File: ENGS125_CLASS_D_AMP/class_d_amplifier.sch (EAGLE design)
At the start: 21 parts, among them J1 BANANA_JACK_CT3151, J2 BANANA_JACK_CT3151, J3 BANANA_JACK_CT3151, J4 BANANA_JACK_CT3151, J5 BANANA_JACK_CT3151, J6 BANANA_JACK_CT3151, M1 AUIRLR024ZTRL, M2 AUIRLR024ZTRL, U1 LTC6992TSOT-23, U2 LTC4449

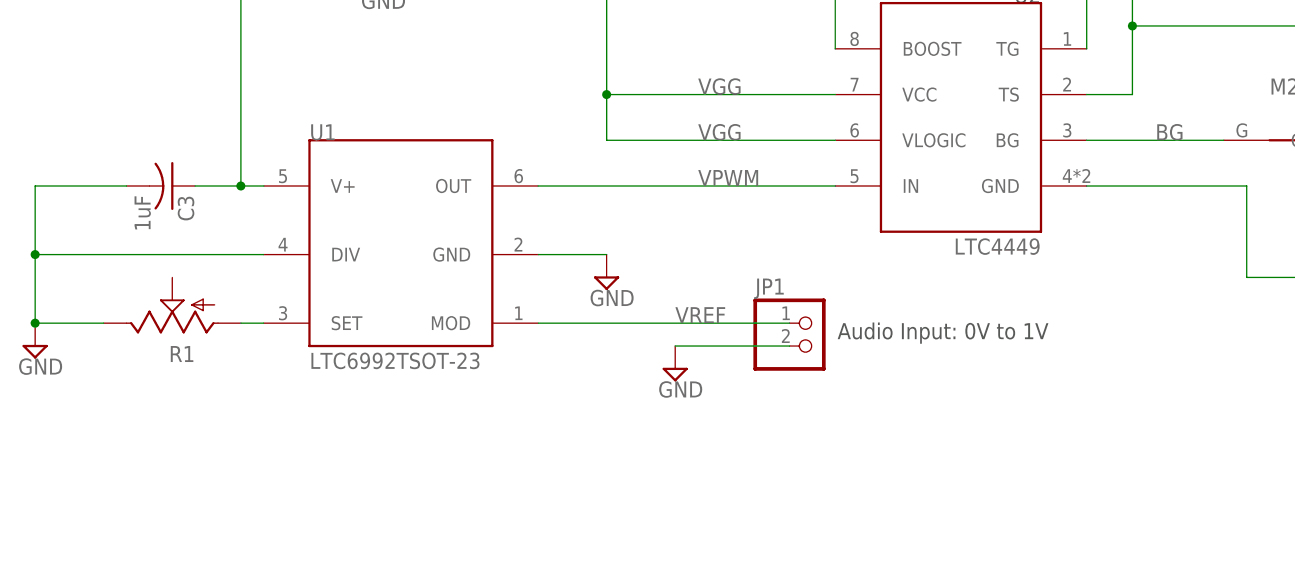
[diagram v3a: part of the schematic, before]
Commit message: Added pin header for PWM output probe
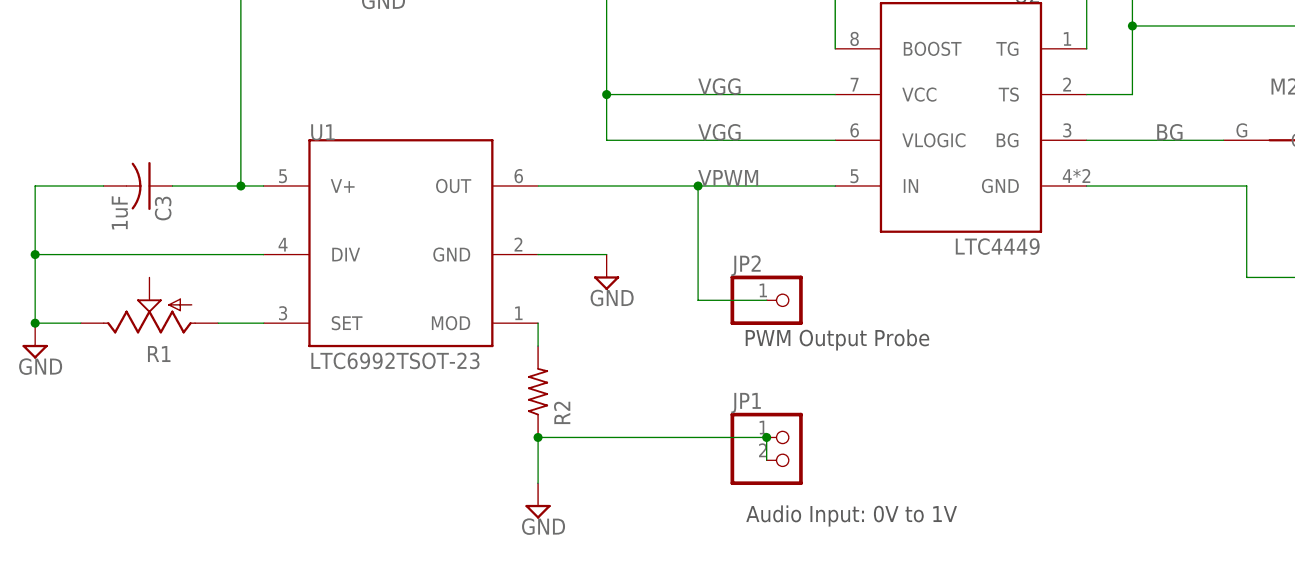
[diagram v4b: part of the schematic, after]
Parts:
- added JP2: (no value), Engs125_lib_UPDATEFeb22:PINHD-1X1
- added R2: R-US, Engs125_lib_UPDATEFeb22:R-US
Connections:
- removed net VREF: JP1.1, U1.MOD
- new net N$4: R2.2, U1.MOD
- net GND: now also JP1.1, R2.1
- net VPWM: now also JP2.1
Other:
- note added: "PWM Output Probe"
- moved on the sheet: C3, JP1, R1
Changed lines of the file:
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@@
 <part name="U1" library="Engs125_lib_UPDATEFeb22" deviceset="LTC6992" device="TSOT-23"/>
 <part name="R1" library="Engs125_lib_UPDATEFeb22" deviceset="TRIM_US-" device="CT6"/>
+<part name="R2" library="Engs125_lib_UPDATEFeb22" deviceset="R-US" device="" value=""/>
+<part name="JP2" library="Engs125_lib_UPDATEFeb22" deviceset="PINHD-1X1" device=""/>
 </parts>
 <sheets>
@@
 @1.5A DC load current (4Ω load)</text>
 <text x="15.24" y="132.08" size="1.778" layer="97">Gate Supply: 5V</text>
-<text x="68.834" y="43.942" size="1.778" layer="97">Audio Input: 0V to 1V</text>
+<text x="58.674" y="23.622" size="1.778" layer="97">Audio Input: 0V to 1V</text>
+<text x="58.42" y="43.18" size="1.778" layer="97">PWM Output Probe</text>
 </plain>
 <instances>
@@
 <attribute name="VALUE" x="-22.225" y="40.005" size="1.778" layer="96"/>
 </instance>
-<instance part="C3" gate="G$1" x="-5.08" y="60.96" smashed="yes" rot="R270">
-<attribute name="NAME" x="-4.445" y="59.944" size="1.778" layer="95" rot="R270"/>
-<attribute name="VALUE" x="-9.271" y="59.944" size="1.778" layer="96" rot="R270"/>
+<instance part="C3" gate="G$1" x="-7.62" y="60.96" smashed="yes" rot="R270">
+<attribute name="NAME" x="-6.985" y="59.944" size="1.778" layer="95" rot="R270"/>
+<attribute name="VALUE" x="-11.811" y="59.944" size="1.778" layer="96" rot="R270"/>
 </instance>
 <instance part="C4" gate="G$1" x="17.78" y="93.98" smashed="yes">
@@
 <attribute name="VALUE" x="41.275" y="47.625" size="1.778" layer="96"/>
 </instance>
-<instance part="SUPPLY3" gate="GND" x="50.8" y="40.64" smashed="yes">
-<attribute name="VALUE" x="48.895" y="37.465" size="1.778" layer="96"/>
+<instance part="SUPPLY3" gate="GND" x="35.56" y="25.4" smashed="yes">
+<attribute name="VALUE" x="33.655" y="22.225" size="1.778" layer="96"/>
 </instance>
 <instance part="SUPPLY4" gate="GND" x="25.4" y="106.68" smashed="yes">
@@
 <attribute name="VALUE" x="168.656" y="66.929" size="1.778" layer="96"/>
 </instance>
-<instance part="JP1" gate="G$1" x="66.04" y="43.18" smashed="yes">
-<attribute name="NAME" x="59.69" y="48.895" size="1.778" layer="95"/>
-<attribute name="VALUE" x="59.69" y="38.1" size="1.778" layer="96"/>
+<instance part="JP1" gate="G$1" x="63.5" y="30.48" smashed="yes">
+<attribute name="NAME" x="57.15" y="36.195" size="1.778" layer="95"/>
+<attribute name="VALUE" x="57.15" y="25.4" size="1.778" layer="96"/>
 </instance>
 <instance part="J1" gate="G$1" x="17.78" y="119.38" smashed="yes" rot="R270">
@@
 <attribute name="VALUE" x="10.16" y="40.64" size="1.778" layer="96"/>
 </instance>
-<instance part="R1" gate="G$1" x="-5.08" y="45.72" smashed="yes" rot="R90">
-<attribute name="NAME" x="-2.54" y="43.18" size="1.778" layer="95" rot="R180"/>
-<attribute name="VALUE" x="-2.54" y="43.18" size="1.778" layer="96" rot="R180"/>
+<instance part="R1" gate="G$1" x="-7.62" y="45.72" smashed="yes" rot="R90">
+<attribute name="NAME" x="-5.08" y="43.18" size="1.778" layer="95" rot="R180"/>
+<attribute name="VALUE" x="-5.08" y="43.18" size="1.778" layer="96" rot="R180"/>
+</instance>
+<instance part="R2" gate="G$1" x="35.56" y="38.1" smashed="yes" rot="R90">
+<attribute name="NAME" x="39.1414" y="34.29" size="1.778" layer="95" rot="R90"/>
+<attribute name="VALUE" x="38.862" y="34.29" size="1.778" layer="96" rot="R90"/>
+</instance>
+<instance part="JP2" gate="G$1" x="63.5" y="48.26" smashed="yes">
+<attribute name="NAME" x="57.15" y="51.435" size="1.778" layer="95"/>
+<attribute name="VALUE" x="57.15" y="43.18" size="1.778" layer="96"/>
 </instance>
 </instances>
@@
 <net name="N$1" class="0">
 <segment>
-<wire x1="5.08" y1="45.72" x2="2.54" y2="45.72" width="0.1524" layer="91"/>
+<wire x1="5.08" y1="45.72" x2="0" y2="45.72" width="0.1524" layer="91"/>
 <pinref part="U1" gate="G$1" pin="SET"/>
 <pinref part="R1" gate="G$1" pin="A"/>
@@
 <segment>
 <pinref part="SUPPLY1" gate="GND" pin="GND"/>
-<wire x1="-12.7" y1="45.72" x2="-20.32" y2="45.72" width="0.1524" layer="91"/>
+<wire x1="-15.24" y1="45.72" x2="-20.32" y2="45.72" width="0.1524" layer="91"/>
 <wire x1="5.08" y1="53.34" x2="-20.32" y2="53.34" width="0.1524" layer="91"/>
 <wire x1="-20.32" y1="53.34" x2="-20.32" y2="45.72" width="0.1524" layer="91"/>
 <junction x="-20.32" y="45.72"/>
 <pinref part="C3" gate="G$1" pin="2"/>
-<wire x1="-10.16" y1="60.96" x2="-20.32" y2="60.96" width="0.1524" layer="91"/>
+<wire x1="-12.7" y1="60.96" x2="-20.32" y2="60.96" width="0.1524" layer="91"/>
 <wire x1="-20.32" y1="60.96" x2="-20.32" y2="53.34" width="0.1524" layer="91"/>
 <junction x="-20.32" y="53.34"/>
@@
 </segment>
 <segment>
-<pinref part="SUPPLY3" gate="GND" pin="GND"/>
-<wire x1="50.8" y1="43.18" x2="63.5" y2="43.18" width="0.1524" layer="91"/>
-<pinref part="JP1" gate="G$1" pin="2"/>
-</segment>
-<segment>
 <pinref part="J2" gate="G$1" pin="IN"/>
 <pinref part="SUPPLY4" gate="GND" pin="GND"/>
@@
 <wire x1="137.16" y1="137.16" x2="137.16" y2="134.62" width="0.1524" layer="91"/>
 </segment>
+<segment>
+<pinref part="JP1" gate="G$1" pin="2"/>
+<pinref part="JP1" gate="G$1" pin="1"/>
+<wire x1="60.96" y1="33.02" x2="60.96" y2="30.48" width="0.1524" layer="91"/>
+<pinref part="R2" gate="G$1" pin="1"/>
+<wire x1="35.56" y1="33.02" x2="60.96" y2="33.02" width="0.1524" layer="91"/>
+<junction x="60.96" y="33.02"/>
+<pinref part="SUPPLY3" gate="GND" pin="GND"/>
+<wire x1="35.56" y1="33.02" x2="35.56" y2="27.94" width="0.1524" layer="91"/>
+<junction x="35.56" y="33.02"/>
+</segment>
 </net>
 <net name="VGG" class="0">
@@
 <pinref part="C3" gate="G$1" pin="1"/>
 <wire x1="5.08" y1="60.96" x2="2.54" y2="60.96" width="0.1524" layer="91"/>
-<wire x1="2.54" y1="60.96" x2="-2.54" y2="60.96" width="0.1524" layer="91"/>
+<wire x1="2.54" y1="60.96" x2="-5.08" y2="60.96" width="0.1524" layer="91"/>
 <wire x1="2.54" y1="60.96" x2="2.54" y2="99.06" width="0.1524" layer="91"/>
 <wire x1="2.54" y1="99.06" x2="17.78" y2="99.06" width="0.1524" layer="91"/>
@@
 <segment>
 <pinref part="U2" gate="G$1" pin="IN"/>
-<wire x1="35.56" y1="60.96" x2="68.58" y2="60.96" width="0.1524" layer="91"/>
+<wire x1="35.56" y1="60.96" x2="53.34" y2="60.96" width="0.1524" layer="91"/>
 <label x="53.34" y="60.96" size="1.778" layer="95"/>
 <pinref part="U1" gate="G$1" pin="OUT"/>
+<pinref part="JP2" gate="G$1" pin="1"/>
+<wire x1="53.34" y1="60.96" x2="68.58" y2="60.96" width="0.1524" layer="91"/>
+<wire x1="53.34" y1="60.96" x2="53.34" y2="48.26" width="0.1524" layer="91"/>
+<wire x1="53.34" y1="48.26" x2="60.96" y2="48.26" width="0.1524" layer="91"/>
+<junction x="53.34" y="60.96"/>
 </segment>
 </net>
@@
 </segment>
 </net>
-<net name="VREF" class="0">
-<segment>
-<wire x1="35.56" y1="45.72" x2="63.5" y2="45.72" width="0.1524" layer="91"/>
-<label x="50.8" y="45.72" size="1.778" layer="95"/>
-<pinref part="JP1" gate="G$1" pin="1"/>
-<pinref part="U1" gate="G$1" pin="MOD"/>
-</segment>
-</net>
 <net name="N$3" class="0">
 <segment>
@@
 </segment>
 </net>
+<net name="N$4" class="0">
+<segment>
+<pinref part="U1" gate="G$1" pin="MOD"/>
+<pinref part="R2" gate="G$1" pin="2"/>
+<wire x1="35.56" y1="45.72" x2="35.56" y2="43.18" width="0.1524" layer="91"/>
+</segment>
+</net>

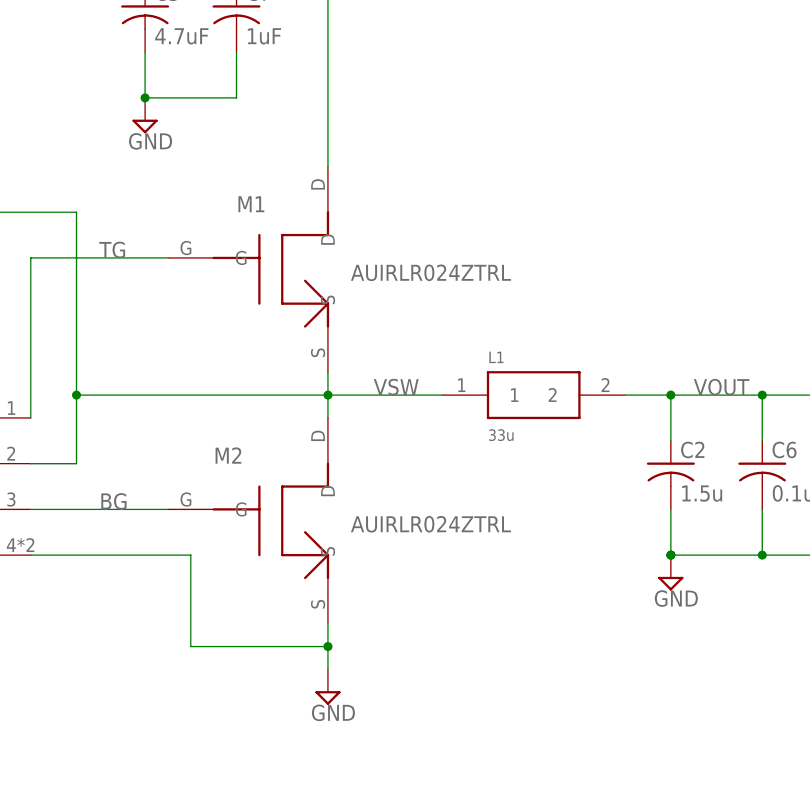
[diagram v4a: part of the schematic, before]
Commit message: Added footprint for switch. Added switch to schematic.
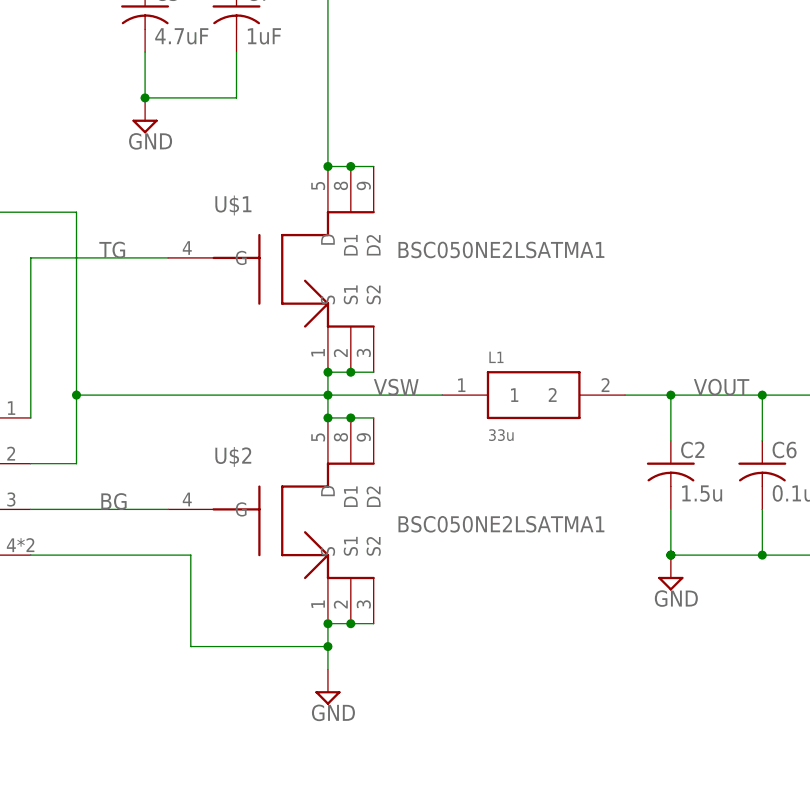
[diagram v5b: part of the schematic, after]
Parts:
- removed M1, M2: AUIRLR024ZTRL, Engs125_library:MOSFET_DPAK
- added U$1, U$2: BSC050NE2LSATMA1, Engs125_lib_UPDATEFeb22:BSC050NE2LSATMA1
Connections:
- net BG: now also U$2.G; no longer M2.G
- net GND: now also U$2.S, U$2.S1, U$2.S2; no longer M2.S
- net TG: now also U$1.G; no longer M1.G
- net VIN: now also U$1.D, U$1.D1, U$1.D2; no longer M1.D
- net VSW: now also U$1.S, U$1.S1, U$1.S2, U$2.D, U$2.D1, U$2.D2; no longer M1.S, M2.D
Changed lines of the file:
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@@
 <part name="C6" library="Engs125_library" deviceset="C-US" device="" value="0.1u"/>
 <part name="D1" library="Engs125_library" deviceset="DIODE" device="" value="1N5819"/>
-<part name="M1" library="Engs125_library" deviceset="MOSFET_DPAK" device="" value="AUIRLR024ZTRL"/>
-<part name="M2" library="Engs125_library" deviceset="MOSFET_DPAK" device="" value="AUIRLR024ZTRL"/>
 <part name="L1" library="Engs125_library" deviceset="SER2900" device="SER" value="33u"/>
 <part name="SUPPLY2" library="Engs125_library" deviceset="GND" device=""/>
@@
 <part name="R2" library="Engs125_lib_UPDATEFeb22" deviceset="R-US" device="" value=""/>
 <part name="JP2" library="Engs125_lib_UPDATEFeb22" deviceset="PINHD-1X1" device=""/>
+<part name="U$1" library="Engs125_lib_UPDATEFeb22" deviceset="BSC050NE2LSATMA1" device=""/>
+<part name="U$2" library="Engs125_lib_UPDATEFeb22" deviceset="BSC050NE2LSATMA1" device=""/>
 </parts>
 <sheets>
@@
 <attribute name="NAME" x="55.88" y="88.9" size="1.778" layer="95"/>
 </instance>
-<instance part="M1" gate="G$1" x="124.46" y="93.98" smashed="yes">
-<attribute name="NAME" x="119.38" y="99.06" size="1.778" layer="95"/>
-<attribute name="VALUE" x="132.08" y="91.44" size="1.778" layer="96"/>
-</instance>
-<instance part="M2" gate="G$1" x="124.46" y="66.04" smashed="yes">
-<attribute name="NAME" x="116.84" y="71.12" size="1.778" layer="95"/>
-<attribute name="VALUE" x="132.08" y="63.5" size="1.778" layer="96"/>
-</instance>
 <instance part="L1" gate="G$1" x="152.4" y="78.74" smashed="yes">
 <attribute name="VALUE" x="147.32" y="73.66" size="1.27" layer="96"/>
@@
 <attribute name="NAME" x="57.15" y="51.435" size="1.778" layer="95"/>
 <attribute name="VALUE" x="57.15" y="43.18" size="1.778" layer="96"/>
+</instance>
+<instance part="U$1" gate="G$1" x="124.46" y="93.98" smashed="yes">
+<attribute name="NAME" x="116.84" y="99.06" size="1.778" layer="96"/>
+<attribute name="VALUE" x="137.16" y="93.98" size="1.778" layer="96"/>
+</instance>
+<instance part="U$2" gate="G$1" x="124.46" y="66.04" smashed="yes">
+<attribute name="NAME" x="116.84" y="71.12" size="1.778" layer="96"/>
+<attribute name="VALUE" x="137.16" y="63.5" size="1.778" layer="96"/>
 </instance>
 </instances>
@@
 </segment>
 <segment>
-<pinref part="M2" gate="G$1" pin="S"/>
 <wire x1="129.54" y1="53.34" x2="129.54" y2="50.8" width="0.1524" layer="91"/>
 <pinref part="SUPPLY9" gate="GND" pin="GND"/>
@@
 <wire x1="96.52" y1="60.96" x2="114.3" y2="60.96" width="0.1524" layer="91"/>
 <wire x1="114.3" y1="60.96" x2="114.3" y2="50.8" width="0.1524" layer="91"/>
+<pinref part="U$2" gate="G$1" pin="S"/>
+<pinref part="U$2" gate="G$1" pin="S2"/>
+<wire x1="134.62" y1="53.34" x2="132.08" y2="53.34" width="0.1524" layer="91"/>
+<junction x="129.54" y="53.34"/>
+<pinref part="U$2" gate="G$1" pin="S1"/>
+<wire x1="132.08" y1="53.34" x2="129.54" y2="53.34" width="0.1524" layer="91"/>
+<junction x="132.08" y="53.34"/>
 </segment>
 <segment>
@@
 <net name="VSW" class="0">
 <segment>
-<pinref part="M1" gate="G$1" pin="S"/>
-<pinref part="M2" gate="G$1" pin="D"/>
 <wire x1="129.54" y1="81.28" x2="129.54" y2="78.74" width="0.1524" layer="91"/>
 <pinref part="L1" gate="G$1" pin="1"/>
@@
 <junction x="101.6" y="78.74"/>
 <label x="134.62" y="78.74" size="1.778" layer="95"/>
+<pinref part="U$1" gate="G$1" pin="S"/>
+<pinref part="U$2" gate="G$1" pin="D"/>
+<pinref part="U$2" gate="G$1" pin="D2"/>
+<wire x1="134.62" y1="76.2" x2="132.08" y2="76.2" width="0.1524" layer="91"/>
+<junction x="129.54" y="76.2"/>
+<pinref part="U$2" gate="G$1" pin="D1"/>
+<wire x1="132.08" y1="76.2" x2="129.54" y2="76.2" width="0.1524" layer="91"/>
+<junction x="132.08" y="76.2"/>
+<pinref part="U$1" gate="G$1" pin="S2"/>
+<wire x1="134.62" y1="81.28" x2="132.08" y2="81.28" width="0.1524" layer="91"/>
+<junction x="129.54" y="81.28"/>
+<pinref part="U$1" gate="G$1" pin="S1"/>
+<wire x1="132.08" y1="81.28" x2="129.54" y2="81.28" width="0.1524" layer="91"/>
+<junction x="132.08" y="81.28"/>
 </segment>
 </net>
@@
 <wire x1="119.38" y1="129.54" x2="119.38" y2="124.46" width="0.1524" layer="91"/>
 <junction x="119.38" y="129.54"/>
-<pinref part="M1" gate="G$1" pin="D"/>
 <wire x1="129.54" y1="129.54" x2="129.54" y2="104.14" width="0.1524" layer="91"/>
 <junction x="129.54" y="129.54"/>
@@
 <wire x1="109.22" y1="129.54" x2="109.22" y2="124.46" width="0.1524" layer="91"/>
 <pinref part="J3" gate="G$1" pin="IN"/>
+<pinref part="U$1" gate="G$1" pin="D"/>
+<pinref part="U$1" gate="G$1" pin="D2"/>
+<wire x1="134.62" y1="104.14" x2="132.08" y2="104.14" width="0.1524" layer="91"/>
+<junction x="129.54" y="104.14"/>
+<pinref part="U$1" gate="G$1" pin="D1"/>
+<wire x1="132.08" y1="104.14" x2="129.54" y2="104.14" width="0.1524" layer="91"/>
+<junction x="132.08" y="104.14"/>
 </segment>
 </net>
@@
 <segment>
 <pinref part="U2" gate="G$1" pin="BG"/>
-<pinref part="M2" gate="G$1" pin="G"/>
 <wire x1="96.52" y1="66.04" x2="111.76" y2="66.04" width="0.1524" layer="91"/>
 <label x="104.14" y="66.04" size="1.778" layer="95"/>
+<pinref part="U$2" gate="G$1" pin="G"/>
 </segment>
 </net>
@@
 <pinref part="U2" gate="G$1" pin="TG"/>
 <wire x1="96.52" y1="76.2" x2="96.52" y2="93.98" width="0.1524" layer="91"/>
-<pinref part="M1" gate="G$1" pin="G"/>
 <wire x1="96.52" y1="93.98" x2="111.76" y2="93.98" width="0.1524" layer="91"/>
 <label x="104.14" y="93.98" size="1.778" layer="95"/>
-</segment>
-</net>
+<pinref part="U$1" gate="G$1" pin="G"/>
+</segment>
+</net>
